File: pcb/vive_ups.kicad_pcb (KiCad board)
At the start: 2 copper layers, 78.2 x 63.5 mm, 47 parts, among them J1 USB_A, J2 USB_B_Micro, J3 Conn_01x04, J4 USB_A, Q1 2N3906, Q2 DMN2020LSN, Q3 DMN2020LSN, SW1 SW_DPDT_x2, U2 FS312F-G, U3 FS8205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

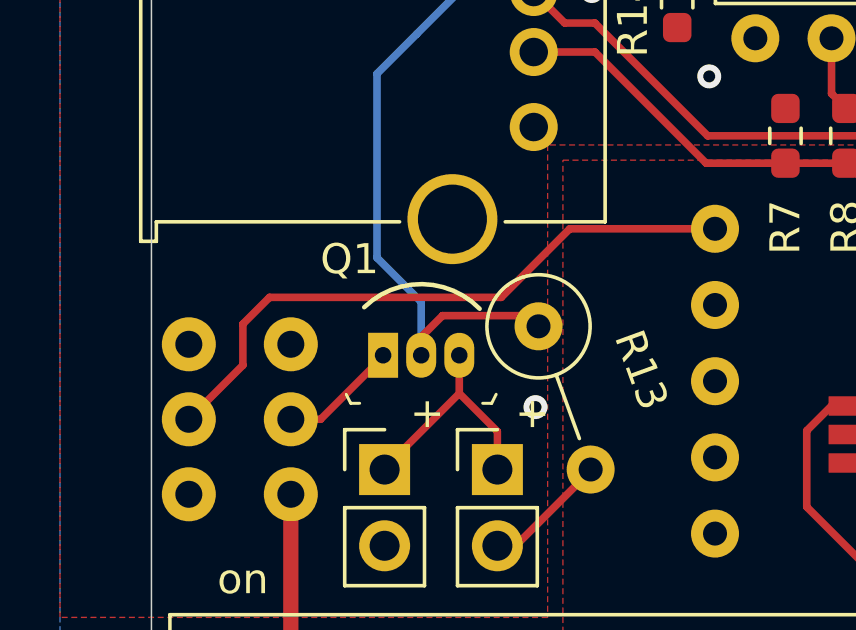
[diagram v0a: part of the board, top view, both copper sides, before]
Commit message: swapped buzzer transistor to equivalent fet (oops)
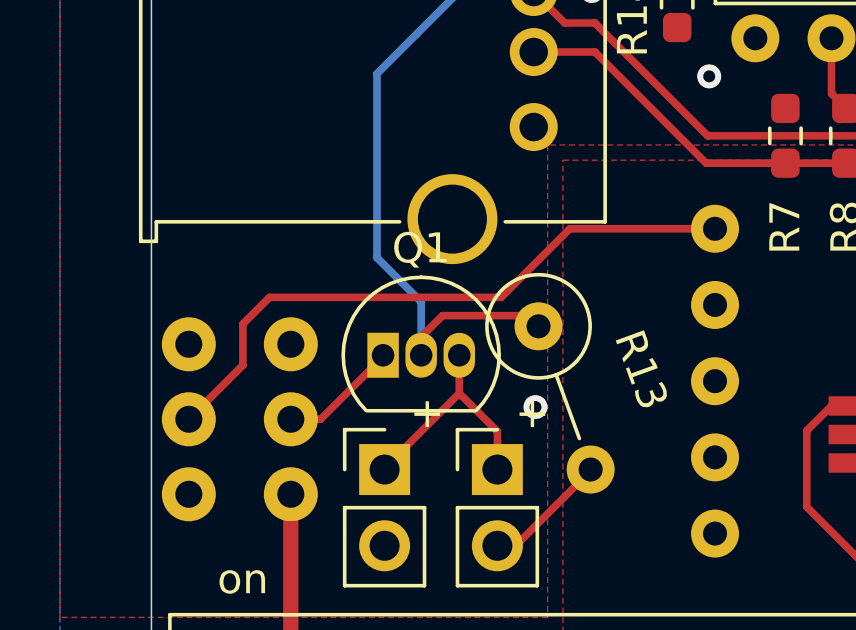
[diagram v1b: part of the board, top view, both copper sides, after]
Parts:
- Q1: value 2N3906 -> BS250; footprint digikey-footprints:TO-92-3 -> Package_TO_SOT_THT:TO-92_Inline
- R13: value 1k -> 10k
